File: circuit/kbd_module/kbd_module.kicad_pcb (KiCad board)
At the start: 2 copper layers, 50 x 50 mm, 25 parts, among them SW1 SW_SIMPLE, SW10 SW_SIMPLE, SW11 SW_SIMPLE, SW12 SW_SIMPLE, SW2 SW_SIMPLE, SW3 SW_SIMPLE, SW4 SW_SIMPLE, SW5 SW_SIMPLE, SW6 SW_SIMPLE, SW7 SW_SIMPLE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

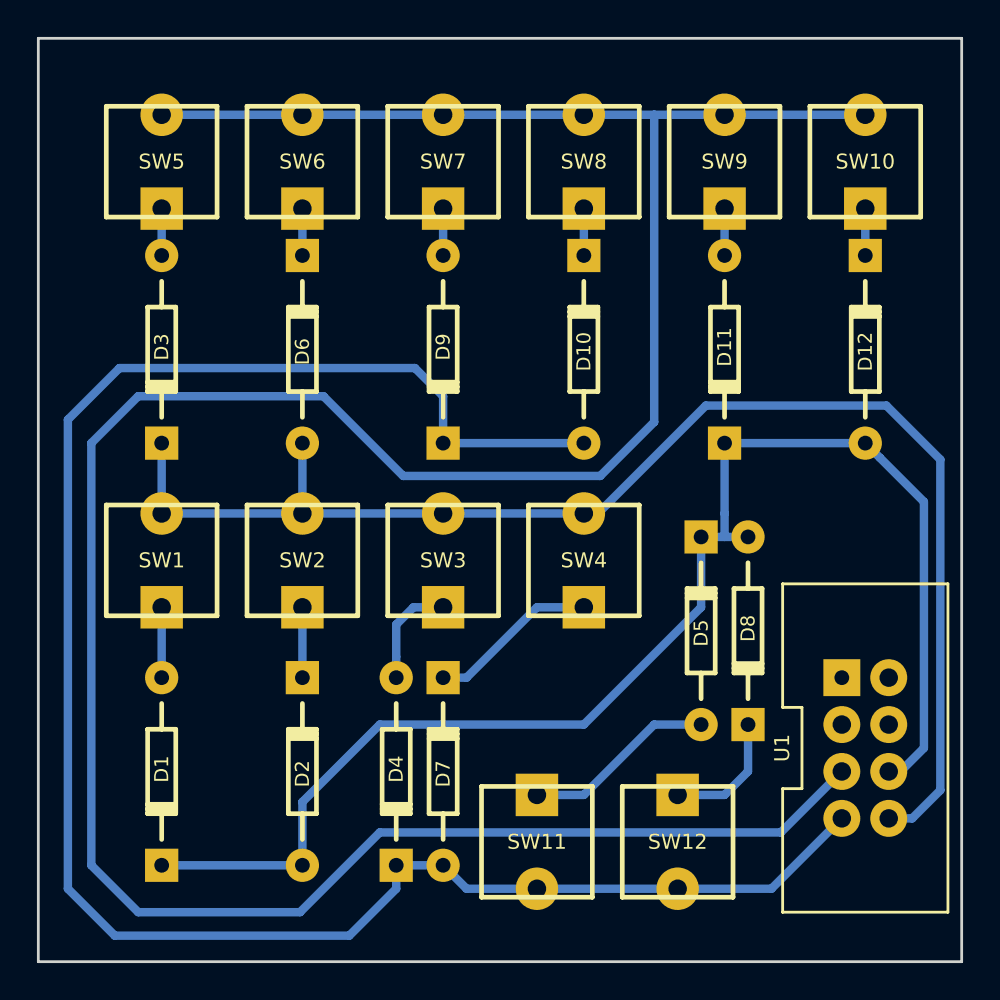
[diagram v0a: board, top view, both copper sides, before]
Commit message: kbd_module diode correction
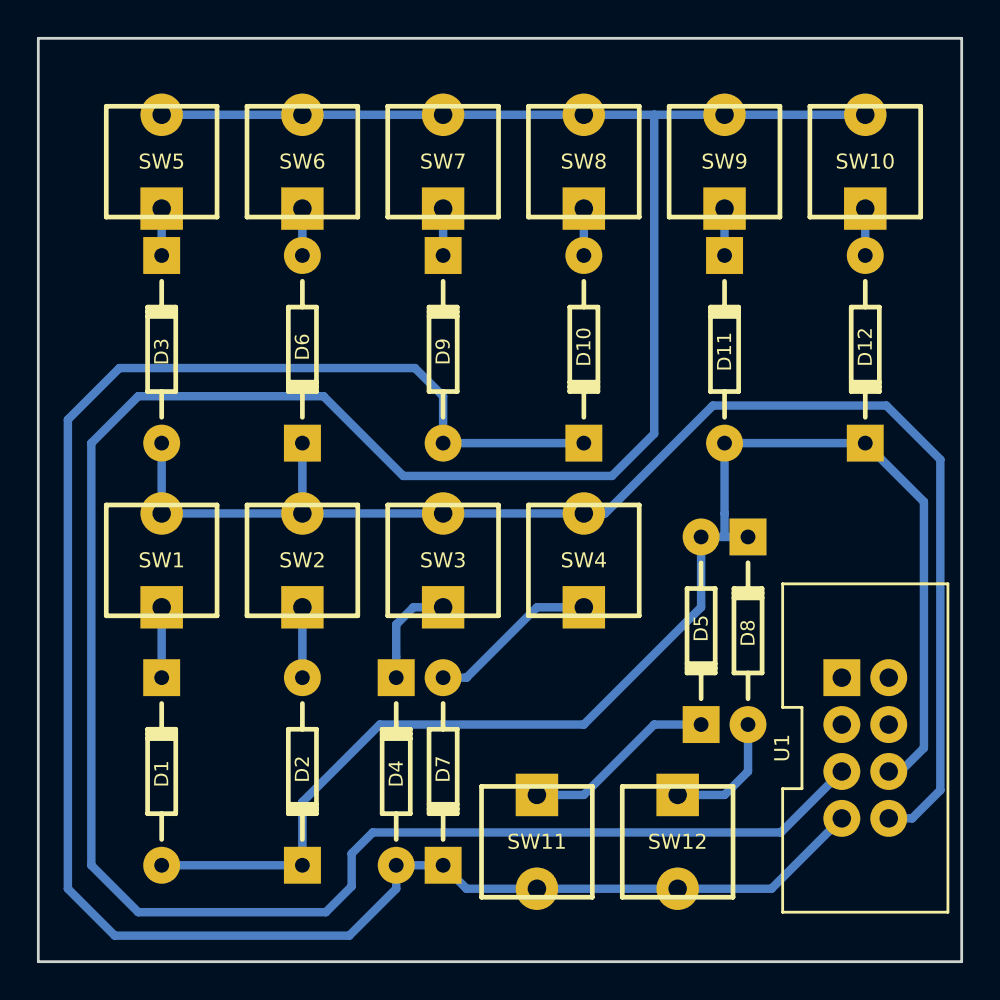
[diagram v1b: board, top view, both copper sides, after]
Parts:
- turned D1 to 90 degrees
- turned D10 to 270 degrees
- turned D11 to 90 degrees
- turned D12 to 270 degrees
- turned D2 to 270 degrees
- turned D3 to 90 degrees
- turned D4 to 90 degrees
- turned D5 to 270 degrees
- turned D6 to 270 degrees
- turned D7 to 270 degrees
- turned D8 to 90 degrees
- turned D9 to 90 degrees
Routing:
- net /FSCK: track 157.0 -> 158.4 mm

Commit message: dual diodes
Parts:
- added D13: 1n4148, kbd_module:SOD27_RM5_5, F.Cu at (105.4, 141.6)
- added D14: 1n4148, kbd_module:SOD27_RM5_5, F.Cu at (113.7, 141.6)
- added D15: 1n4148, kbd_module:SOD27_RM5_5, F.Cu at (108.0, 114.9)
- added D16: 1n4148, kbd_module:SOD27_RM5_5, F.Cu at (120.7, 142.2)
- added D17: 1n4148, kbd_module:SOD27_RM5_5, F.Cu at (144.8, 123.2)
- added D18: 1n4148, kbd_module:SOD27_RM5_5, F.Cu at (115.6, 114.9)
- added D19: 1n4148, kbd_module:SOD27_RM5_5, F.Cu at (128.3, 135.9)
- added D20: 1n4148, kbd_module:SOD27_RM5_5, F.Cu at (138.4, 125.1)
- added D21: 1n4148, kbd_module:SOD27_RM5_5, F.Cu at (120.7, 120.0)
- added D22: 1n4148, kbd_module:SOD27_RM5_5, F.Cu at (128.3, 120.0)
- added D23: 1n4148, kbd_module:SOD27_RM5_5, F.Cu at (135.9, 120.0)
- added D24: 1n4148, kbd_module:SOD27_RM5_5, F.Cu at (142.9, 117.5)
- D1, D10, D11, D12, D2, D3, D4, D5, D6, D7, D8, D9: value D -> 1n4148; footprint kbd_module:Diode_DO-35_SOD27_Horizontal_RM10 -> kbd_module:SOD27_RM5_5
- SW1, SW10, SW11, SW12, SW2, SW3, SW4, SW5, SW6, SW7, SW8, SW9: footprint kbd_module:Tact_6x6 -> kbd_module:ExtSwitch
- moved D5 10.2 mm to (144.8, 127.0), turned to 180 degrees
- moved D7 9.67 mm to (130.8, 135.9)
- moved D4 4.58 mm to (123.2, 137.2)
- moved D2 3.70 mm to (116.2, 136.5)
- moved D3 3.42 mm to (105.4, 120.0)
- moved D6 3.42 mm to (113.0, 120.0)
- moved D1 3.42 mm to (108.0, 136.5)
- moved D8 3.18 mm to (135.9, 130.2)
- moved D10 2.29 mm to (130.8, 114.9)
- moved D11 2.29 mm to (138.4, 114.9)
- moved D12 2.29 mm to (146.1, 114.9)
- moved D9 2.29 mm to (123.2, 114.9)
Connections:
- D1 pad 2: /FMOSI -> Net-(D1-Pad2)
- D10 pad 1: /FMISO -> Net-(D10-Pad1)
- D11 pad 2: /FMOSI -> Net-(D11-Pad2)
- D12 pad 1: /FMOSI -> Net-(D12-Pad1)
- D2 pad 1: /FMOSI -> Net-(D14-Pad2)
- D3 pad 1: Net-(D3-Pad1) -> Net-(D15-Pad2)
- D4 pad 2: /FMISO -> Net-(D16-Pad1)
- D5 pad 2: /FMOSI -> Net-(D17-Pad1)
- D6 pad 2: Net-(D6-Pad2) -> Net-(D18-Pad1)
- D7 pad 1: /FMISO -> Net-(D19-Pad2)
- D8 pad 1: /FMOSI -> Net-(D20-Pad2)
- D9 pad 2: /FMISO -> Net-(D21-Pad1)
- SW5 pad 1: Net-(D3-Pad1) -> Net-(D15-Pad1)
- SW6 pad 1: Net-(D6-Pad2) -> Net-(D18-Pad2)
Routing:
- net /FSCK: track 158.4 -> 84.4 mm
- net /FMISO: track 105.1 -> 65.3 mm
- net Net-(D5-Pad1): track 10.5 -> 26.7 mm
- net /FCSN: track 74.7 -> 83.8 mm
- net /FMOSI: track 76.3 -> 82.5 mm
- net Net-(D12-Pad1): track 0.00 -> 5.34 mm
- net Net-(D18-Pad2): track 0.00 -> 4.97 mm
- net Net-(D15-Pad1): track 0.00 -> 4.97 mm
- net Net-(D7-Pad2): track 9.20 -> 4.34 mm
- net Net-(D17-Pad1): track 0.00 -> 3.81 mm
- net Net-(D8-Pad2): track 6.88 -> 10.1 mm
- net Net-(D20-Pad2): track 0.00 -> 2.54 mm
- net Net-(D11-Pad2): track 0.00 -> 2.54 mm
- net Net-(D6-Pad2): track 2.54 -> 0.00 mm
- net Net-(D3-Pad1): track 2.54 -> 0.00 mm
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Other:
- board size 50 x 50 mm -> 46.5 x 48 mm

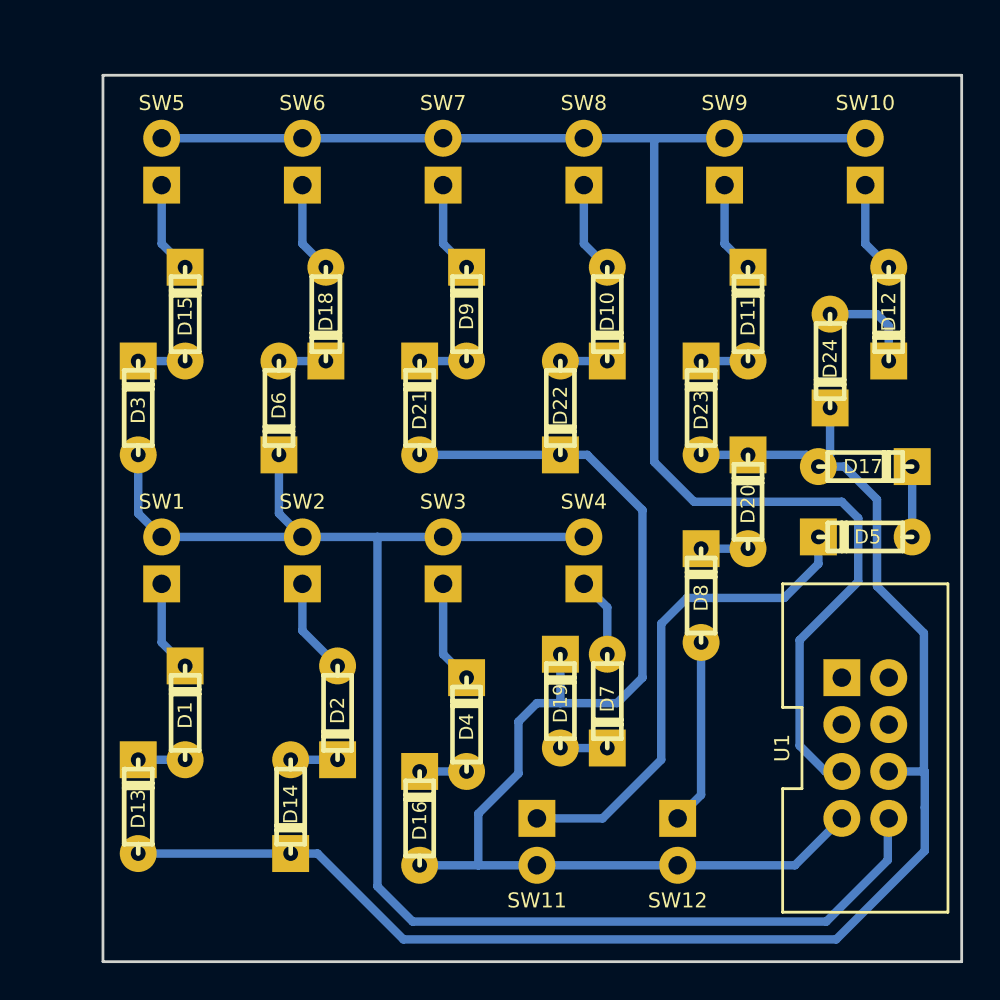
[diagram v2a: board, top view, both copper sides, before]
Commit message: moved the diodes from the edge
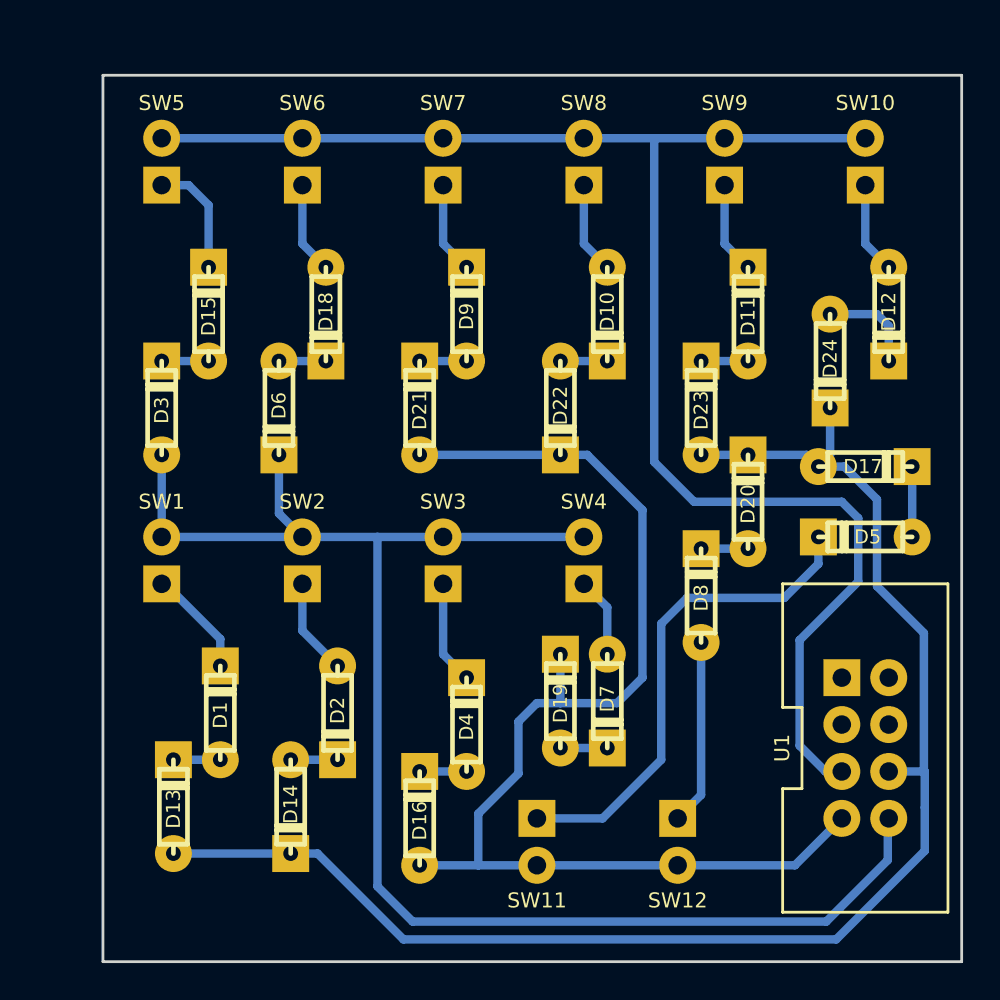
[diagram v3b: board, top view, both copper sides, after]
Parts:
- moved D1 1.91 mm to (109.9, 136.5)
- moved D13 1.91 mm to (107.3, 141.6)
- moved D3 1.27 mm to (106.7, 120.0)
- moved D15 1.27 mm to (109.2, 114.9)
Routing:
- net /FMOSI: track 82.5 -> 80.6 mm
- net Net-(D15-Pad1): track 4.97 -> 6.35 mm
- net Net-(D1-Pad1): track 4.97 -> 5.87 mm
- net /FCSN: track 83.8 -> 83.3 mm
- added copper zone on F.Cu, net (none)
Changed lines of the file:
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@@
     (thickness 1.6)
     (drawings 4)
-    (tracks 108)
+    (tracks 109)
     (zones 0)
     (modules 37)
@@
     (last_trace_width 0.4572)
     (trace_clearance 0.254)
-    (zone_clearance 0.8128)
+    (zone_clearance 0.3556)
     (zone_45_only no)
     (trace_min 0.2)
@@
   )
   (module kbd_module:SOD27_RM5_5 (layer F.Cu)
-    (at 107.95 114.935 90)
+    (at 109.22 114.935 90)
     (descr "SOD27, Horizontal, RM 5.5mm")
     (tags "SOD27, Horizontal, RM 5.5mm, 1N4148")
@@
   )
   (module kbd_module:SOD27_RM5_5 (layer F.Cu)
-    (at 105.41 141.605 90)
+    (at 107.315 141.605 90)
     (descr "SOD27, Horizontal, RM 5.5mm")
     (tags "SOD27, Horizontal, RM 5.5mm, 1N4148")
@@
   )
   (module kbd_module:SOD27_RM5_5 (layer F.Cu)
-    (at 105.41 120.015 90)
+    (at 106.68 120.015 90)
     (descr "SOD27, Horizontal, RM 5.5mm")
     (tags "SOD27, Horizontal, RM 5.5mm, 1N4148")
@@
   )
   (module kbd_module:SOD27_RM5_5 (layer F.Cu)
-    (at 107.95 136.525 90)
+    (at 109.855 136.525 90)
     (descr "SOD27, Horizontal, RM 5.5mm")
     (tags "SOD27, Horizontal, RM 5.5mm, 1N4148")
@@
   (gr_line (start 103.5 102) (end 150 102) (angle 90) (layer Edge.Cuts) (width 0.15))
   (gr_line (start 103.5 102) (end 103.5 150) (angle 90) (layer Edge.Cuts) (width 0.15))
-  (segment (start 106.68 129.54) (end 106.68 132.715) (width 0.4572) (layer B.Cu) (net 1))
-  (segment (start 106.68 132.715) (end 107.95 133.985) (width 0.4572) (layer B.Cu) (net 1))
+  (segment (start 109.855 133.985) (end 109.855 132.5278) (width 0.4572) (layer B.Cu) (net 1))
+  (segment (start 109.855 132.5278) (end 106.8672 129.54) (width 0.4572) (layer B.Cu) (net 1))
+  (segment (start 106.8672 129.54) (end 106.68 129.54) (width 0.4572) (layer B.Cu) (net 1))
+  (segment (start 107.315 144.145) (end 113.665 144.145) (width 0.4572) (layer B.Cu) (net 2))
   (segment (start 147.955 139.7) (end 147.955 132.207) (width 0.4572) (layer B.Cu) (net 2))
   (segment (start 143.637 123.19) (end 142.24 123.19) (width 0.4572) (layer B.Cu) (net 2))
@@
   (segment (start 138.43 122.555) (end 141.605 122.555) (width 0.4572) (layer B.Cu) (net 2))
   (segment (start 141.605 122.555) (end 142.24 123.19) (width 0.4572) (layer B.Cu) (net 2))
-  (segment (start 113.665 144.145) (end 105.41 144.145) (width 0.4572) (layer B.Cu) (net 2))
   (segment (start 138.43 122.555) (end 135.89 122.555) (width 0.4572) (layer B.Cu) (net 2))
   (segment (start 114.3 129.54) (end 114.3 132.08) (width 0.4572) (layer B.Cu) (net 3))
   (segment (start 114.3 132.08) (end 116.205 133.985) (width 0.4572) (layer B.Cu) (net 3))
+  (segment (start 106.68 122.555) (end 106.68 127) (width 0.4572) (layer B.Cu) (net 4))
   (segment (start 118.364 127) (end 118.364 145.923) (width 0.4572) (layer B.Cu) (net 4))
   (segment (start 118.364 145.923) (end 120.269 147.828) (width 0.4572) (layer B.Cu) (net 4))
@@
   (segment (start 118.364 127) (end 114.3 127) (width 0.4572) (layer B.Cu) (net 4))
   (segment (start 121.92 127) (end 118.364 127) (width 0.4572) (layer B.Cu) (net 4))
-  (segment (start 105.41 122.555) (end 105.41 125.73) (width 0.4572) (layer B.Cu) (net 4))
-  (segment (start 105.41 125.73) (end 106.68 127) (width 0.4572) (layer B.Cu) (net 4))
   (segment (start 129.54 127) (end 121.92 127) (width 0.4572) (layer B.Cu) (net 4))
   (segment (start 106.68 127) (end 114.3 127) (width 0.4572) (layer B.Cu) (net 4))
@@
   (segment (start 114.3 105.41) (end 121.92 105.41) (width 0.4572) (layer B.Cu) (net 14))
   (segment (start 106.68 105.41) (end 114.3 105.41) (width 0.4572) (layer B.Cu) (net 14))
-  (segment (start 105.41 139.065) (end 107.95 139.065) (width 0.4572) (layer B.Cu) (net 15))
+  (segment (start 109.855 139.065) (end 107.315 139.065) (width 0.4572) (layer B.Cu) (net 15))
   (segment (start 113.665 139.065) (end 116.205 139.065) (width 0.4572) (layer B.Cu) (net 16))
-  (segment (start 107.95 117.475) (end 105.41 117.475) (width 0.4572) (layer B.Cu) (net 17))
+  (segment (start 106.68 117.475) (end 109.22 117.475) (width 0.4572) (layer B.Cu) (net 17))
   (segment (start 120.65 139.7) (end 123.19 139.7) (width 0.4572) (layer B.Cu) (net 18))
   (segment (start 147.32 123.19) (end 147.32 127) (width 0.4572) (layer B.Cu) (net 19))
@@
   (segment (start 145.415 114.935) (end 142.875 114.935) (width 0.4572) (layer B.Cu) (net 26))
   (segment (start 146.05 115.57) (end 145.415 114.935) (width 0.4572) (layer B.Cu) (net 26))
-  (segment (start 106.68 107.95) (end 106.68 111.125) (width 0.4572) (layer B.Cu) (net 27))
-  (segment (start 106.68 111.125) (end 107.95 112.395) (width 0.4572) (layer B.Cu) (net 27))
+  (segment (start 109.22 112.395) (end 109.22 109.0328) (width 0.4572) (layer B.Cu) (net 27))
+  (segment (start 109.22 109.0328) (end 108.1372 107.95) (width 0.4572) (layer B.Cu) (net 27))
+  (segment (start 108.1372 107.95) (end 106.68 107.95) (width 0.4572) (layer B.Cu) (net 27))
   (segment (start 114.3 107.95) (end 114.3 111.125) (width 0.4572) (layer B.Cu) (net 28))
   (segment (start 114.3 111.125) (end 115.57 112.395) (width 0.4572) (layer B.Cu) (net 28))
@@
       )
     )
+  )
+  (zone (net 0) (net_name "") (layer F.Cu) (hatch edge 0.508)
+    (connect_pads (clearance 0.3556))
+    (min_thickness 0.254)
+    (fill yes (arc_segments 16) (thermal_gap 0.508) (thermal_bridge_width 0.508))
+    (polygon
+      (pts
+        (xy 103.5 102) (xy 150 102) (xy 150 150) (xy 103.5 150)
+      )
+    )
